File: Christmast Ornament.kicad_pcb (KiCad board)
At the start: 2 copper layers, 98.8 x 92.8 mm, 3 parts

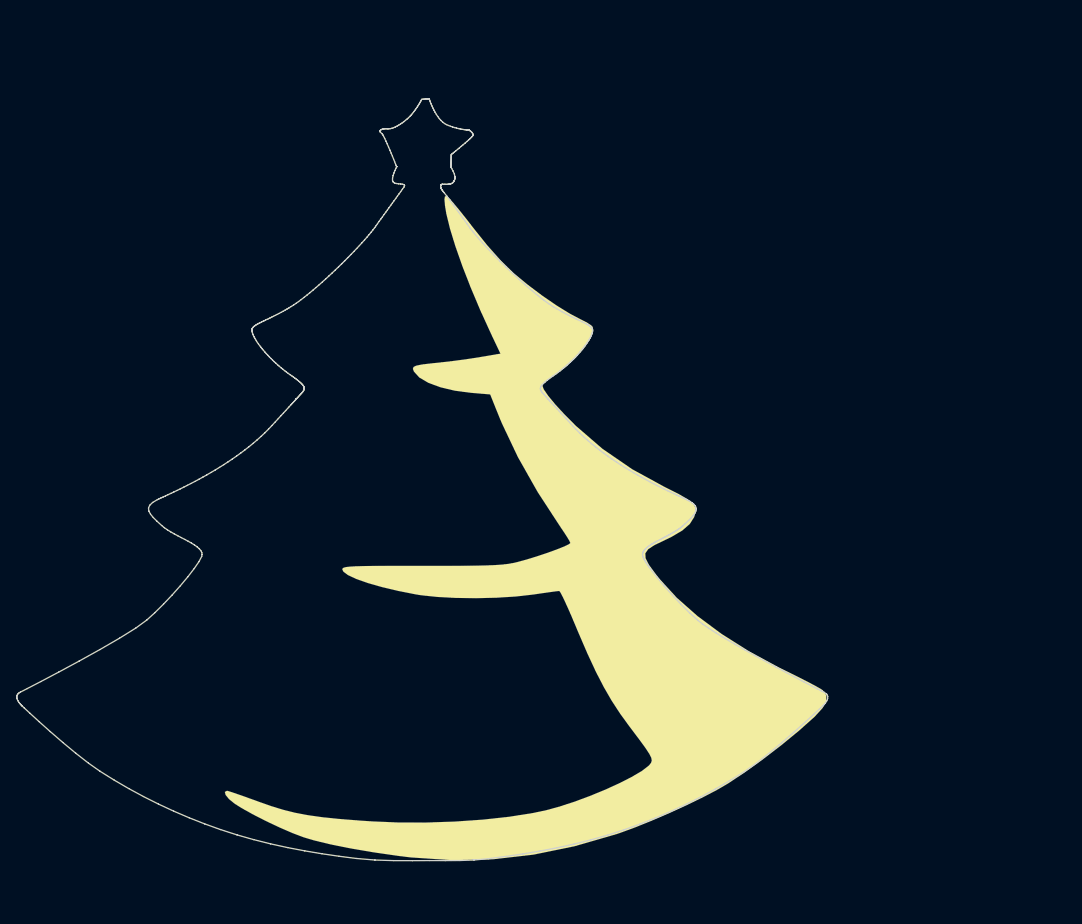
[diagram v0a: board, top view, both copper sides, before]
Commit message: First attempt to distribute components
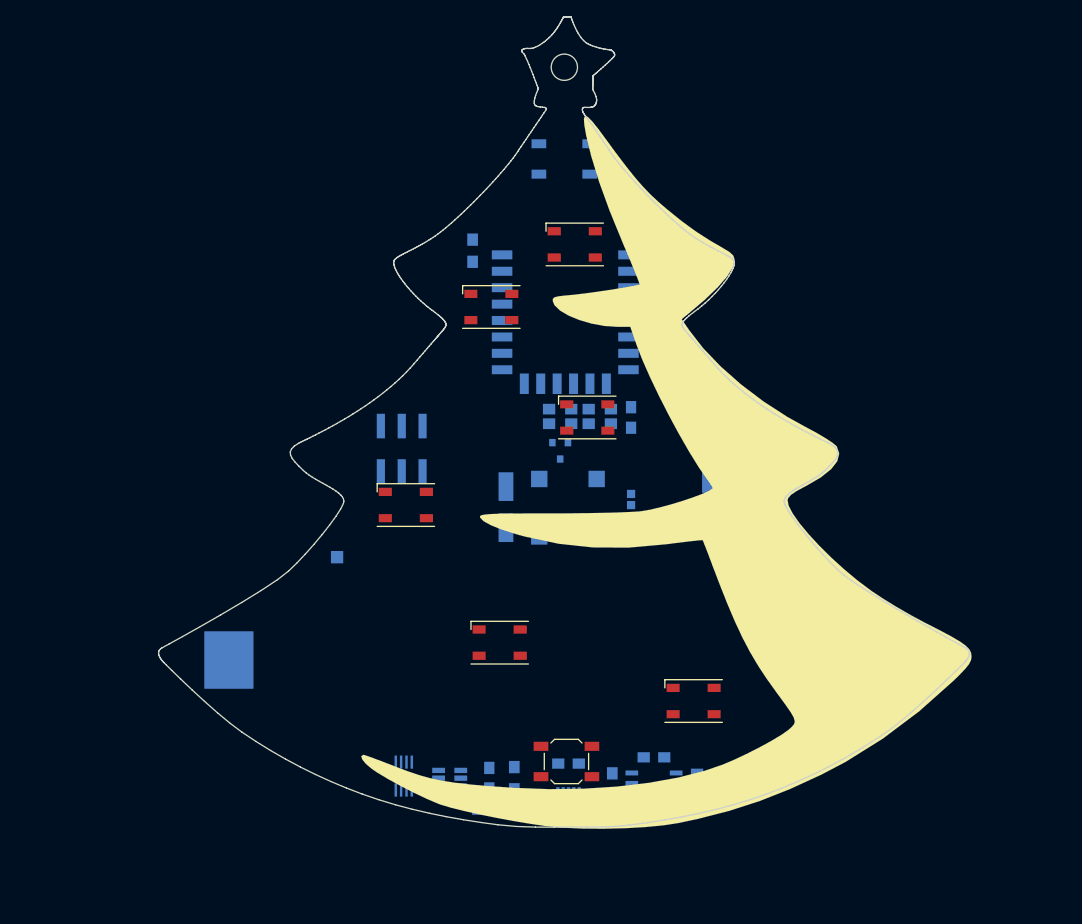
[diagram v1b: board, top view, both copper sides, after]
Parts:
- added BT1: Battery_Cell, MisModulos:18650_SMD_Case, B.Cu at (208.3, 105.7)
- added BZ1: Buzzer, MisModulos:Buzzer_8.5x8.5mm, B.Cu at (164.3, 101.9)
- added C1: 10uF, Capacitors_SMD:C_0805_HandSoldering, B.Cu at (168.7, 128.8)
- added C2: 10uF, Capacitors_SMD:C_0805_HandSoldering, B.Cu at (179.1, 128.0)
- added C3: 0.1uF, Capacitors_SMD:C_0805_HandSoldering, B.Cu at (159.0, 130.6)
- added C4: 1uF, Capacitors_SMD:C_0805_HandSoldering, B.Cu at (190.5, 95.8)
- added C5: 22uF, Capacitors_Tantalum_SMD:CP_Tantalum_Case-A_EIA-3216-18_Hand, B.Cu at (185.7, 92.2)
- added C6: 10uF, Capacitors_SMD:C_0805_HandSoldering, B.Cu at (176.3, 86.6)
- added D1: LED, LEDs:LED_0805, B.Cu at (190.5, 131.3)
- added D2: LED, LEDs:LED_0805, B.Cu at (190.5, 129.3)
- added D3: M7, Diodes_SMD:D_SMA_Handsoldering, B.Cu at (161.0, 97.5)
- added J1: USB_OTG, MisModulos:MicroUSB, B.Cu at (168.7, 135.0)
- added J2: CONN_01X06, Pin_Headers:Pin_Header_Straight_2x03_Pitch2.54mm_SMD, B.Cu at (148.3, 90.4)
- added JP1: Jumper_NC_Dual, MisModulos:Jumper_2-NC, B.Cu at (176.3, 97.3)
- added Q1: 8205A, Housings_SSOP:SSOP-8_2.95x2.8mm_Pitch0.65mm, B.Cu at (148.6, 130.3)
- added Q2: SI2302, TO_SOT_Packages_SMD:SOT-23, B.Cu at (179.8, 74.2)
- added Q3: BC817, TO_SOT_Packages_SMD:SOT-23, B.Cu at (167.6, 90.7)
- added R1: 100, Resistors_SMD:R_0805_HandSoldering, B.Cu at (162.1, 130.6)
- added R10: 10k, Resistors_SMD:R_0805_HandSoldering, B.Cu at (157.0, 66.3)
- added R11: 470, Resistors_SMD:R_0805_HandSoldering, B.Cu at (167.6, 85.6)
- added R12: 10K, Resistors_SMD:R_0805_HandSoldering, B.Cu at (167.6, 87.4)
- added R13: 10K, Resistors_SMD:R_0805_HandSoldering, B.Cu at (180.3, 77.5)
- added R2: 1k, Resistors_SMD:R_0805_HandSoldering, B.Cu at (185.7, 132.1)
- added R3: 1k, Resistors_SMD:R_0805_HandSoldering, B.Cu at (185.7, 130.0)
- added R4: 1k2, Resistors_SMD:R_0805_HandSoldering, B.Cu at (174.0, 131.3)
- added R5: 1k, Resistors_SMD:R_0805_HandSoldering, B.Cu at (159.0, 134.4)
- added R6: 10k, Resistors_SMD:R_0805_HandSoldering, B.Cu at (180.6, 69.3)
- added R7: 10k, Resistors_SMD:R_0805_HandSoldering, B.Cu at (172.5, 87.4)
- added R8: 10k, Resistors_SMD:R_0805_HandSoldering, B.Cu at (172.5, 85.6)
- added R9: 10k, Resistors_SMD:R_0805_HandSoldering, B.Cu at (180.3, 65.5)
- added REF**: MountingHole_3.2mm_M3, Mounting_Holes:MountingHole_3.2mm_M3, F.Cu at (168.1, 43.9)
- added SW1: SW_Push, Buttons_Switches_SMD:SW_SPST_SKQG, B.Cu at (168.1, 55.1)
- added SW2: SW_Push, Buttons_Switches_SMD:SW_SPST_SKQG, F.Cu at (168.4, 128.5)
- added TP1: TEST, Measurement_Points:Measurement_Point_Square-SMD-Pad_Small, B.Cu at (194.8, 129.3)
- added TP2: TEST, Measurement_Points:Measurement_Point_Square-SMD-Pad_Small, B.Cu at (195.6, 103.1)
- added TP3: TEST, Measurement_Points:Measurement_Point_Square-SMD-Pad_Small, B.Cu at (191.0, 103.1)
- added TP4: TEST, Measurement_Points:Measurement_Point_Square-SMD-Pad_Small, B.Cu at (140.5, 103.6)
- added U1: TP4056, Housings_SOIC:SOIC-8_3.9x4.9mm_Pitch1.27mm, B.Cu at (179.1, 131.8)
- added U10: WS2812b, LEDs:LED_WS2812B-PLCC4, F.Cu at (183.9, 121.2)
- added U2: HT7833, TO_SOT_Packages_SMD:SOT89-3_Housing_Handsoldering, B.Cu at (191.0, 91.9)
- added U3: DW01, TO_SOT_Packages_SMD:SOT-23-6_Handsoldering, B.Cu at (154.2, 130.6)
- added U4: ESP-12E, MisModulos:ESP-12E_SMD, B.Cu at (175.3, 66.8)
- added U5: WS2812b, LEDs:LED_WS2812B-PLCC4, F.Cu at (169.4, 65.5)
- added U6: WS2812b, LEDs:LED_WS2812B-PLCC4, F.Cu at (159.3, 73.2)
- added U7: WS2812b, LEDs:LED_WS2812B-PLCC4, F.Cu at (170.9, 86.6)
- added U8: WS2812b, LEDs:LED_WS2812B-PLCC4, F.Cu at (148.8, 97.3)
- added U9: WS2812b, LEDs:LED_WS2812B-PLCC4, F.Cu at (160.3, 114.0)
- moved G*** 33.4 mm to (138.9, 91.7)
- moved G*** 19.6 mm to (168.4, 43.4)
- moved G*** 18.6 mm to (180.6, 93.2)
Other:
- board size 98.8 x 92.8 mm -> 98.8 x 98.7 mm
- board text added: "Revisar pines esp12 ¿Desplazar DW01 y 8205?"

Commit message: PCB routed
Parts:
- removed the REF** at (168.1, 43.9)
- added 3V3: TEST, Measurement_Points:Measurement_Point_Square-SMD-Pad_Small, B.Cu at (183.9, 89.4)
- added GND: TEST, Measurement_Points:Measurement_Point_Square-SMD-Pad_Small, B.Cu at (161.8, 134.9)
- added REF**: MountingHole_2.7mm_M2.5, Mounting_Holes:MountingHole_2.7mm_M2.5, F.Cu at (168.1, 43.7)
- R4: value 1k2 -> 2k7
- moved R5 42.1 mm to (146.3, 94.2)
- moved D1 40.4 mm to (150.1, 131.3), turned to 90 degrees
- moved J2 40.0 mm to (168.1, 55.6)
- moved D2 38.4 mm to (152.1, 131.3), turned to 90 degrees
- moved U3 33.8 mm to (144.9, 98.0), turned to 270 degrees
- moved Q1 31.9 mm to (149.1, 98.4)
- moved C3 31.4 mm to (143.7, 103.1), turned to 180 degrees
- moved R1 30.6 mm to (148.4, 103.1), turned to 180 degrees
- moved R2 28.2 mm to (157.5, 132.6), turned to 180 degrees
- moved R3 28.2 mm to (157.5, 130.6), turned to 180 degrees
- moved BAT+ 26.2 mm to (195.8, 129.3)
- moved BAT- 25.7 mm to (140.7, 129.3)
- moved VCC 20.1 mm to (175.5, 134.9)
- moved R8 20.1 mm to (152.6, 82.5), turned to 90 degrees
- moved SW1 19.4 mm to (154.4, 68.8)
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- renumbered TP2 to BAT+, TP4 to BAT-, TP3 to GND, TP1 to VCC
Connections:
- J2 pad 1: +3V3 -> GND
- J2 pad 2: /TxD -> +3V3
- J2 pad 3: /RxD -> /TxD
- J2 pad 5: Net-(J2-Pad5) -> /RxD
- J2 pad 6: GND -> Net-(J2-Pad6)
- U7 pad 2: Net-(U10-Pad4) -> Net-(U7-Pad2)
- U8 pad 4: Net-(U8-Pad4) -> Net-(U7-Pad2)
- U9 pad 2: Net-(U8-Pad4) -> Net-(U10-Pad4)
- U9 pad 4: Net-(U10-Pad2) -> Net-(U8-Pad2)
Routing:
- net GND: track 0.00 -> 331.4 mm, vias 0 -> 4
- net +3V3: track 0.00 -> 223.0 mm, vias 0 -> 2
- net /PIX_GND: track 0.00 -> 149.7 mm, vias 0 -> 1
- net /RST: track 0.00 -> 116.0 mm, vias 0 -> 1
- net /BAT+: track 0.00 -> 110.9 mm, vias 0 -> 2
- net /BAT-: track 0.00 -> 64.2 mm
- net /VCC: track 0.00 -> 64.1 mm
- net /PIX_DATA: track 0.00 -> 38.8 mm, vias 0 -> 1
- net Net-(R3-Pad1): track 0.00 -> 31.1 mm, vias 0 -> 2
- net Net-(R2-Pad1): track 0.00 -> 29.3 mm, vias 0 -> 2
- net Net-(U7-Pad2): track 0.00 -> 26.8 mm
- net Net-(Q3-Pad1): track 0.00 -> 23.1 mm
- net /TxD: track 0.00 -> 22.0 mm
- net /RxD: track 0.00 -> 21.5 mm
- net Net-(U5-Pad2): track 0.00 -> 21.1 mm
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- added copper zone on B.Cu, net GND
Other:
- net class Alimentación added: clearance 0.25, trace_width 0.3, via_dia 0.6, via_drill 0.3
- net class Default: clearance 0.2 -> 0.15; trace_width 0.25 -> 0.15; via_dia 0.6 -> 0.3; via_drill 0.4 -> 0.15
- rule trace_clearance: 0.2 -> 0.15
- rule trace_min: 0.2 -> 0.15
- rule via_min_drill: 0.3 -> 0.15
- rule via_min_size: 0.4 -> 0.3
- board text added: "+"
- board text added: "-"
- board text removed: "Revisar pines esp12 ¿Desplazar DW01 y 8205?"

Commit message: PCB designed and gerbers
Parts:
- added C10: 0.1uF, Capacitors_SMD:C_0805_HandSoldering, F.Cu at (149.5, 92.5)
- added C11: 0.1uF, Capacitors_SMD:C_0805_HandSoldering, F.Cu at (160.4, 109.9)
- added C12: 0.1uF, Capacitors_SMD:C_0805_HandSoldering, F.Cu at (182.1, 116.1)
- added C7: 0.1uF, Capacitors_SMD:C_0805_HandSoldering, F.Cu at (168.0, 50.3)
- added C8: 0.1uF, Capacitors_SMD:C_0805_HandSoldering, F.Cu at (159.9, 67.4)
- added C9: 0.1uF, Capacitors_SMD:C_0805_HandSoldering, F.Cu at (169.6, 82.7)
- added G***: LOGO, MisModulos:MerryChristmas, F.Cu at (141.9, 113.3)
- C5: value 22uF -> 2.2uF
- TP1: renamed from VCC; value TEST -> VCC
- TP2, TP6: renamed from GND; value TEST -> GND
- TP3: renamed from BAT+; value TEST -> BAT+
- TP4: renamed from BAT-; value TEST -> BAT-
- TP5: renamed from 3V3; value TEST -> 3V3
- moved G*** 54.7 mm to (195.0, 91.3)
- moved G*** 0.08 mm to (168.4, 43.5)
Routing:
- net +3V3: track 223.0 -> 277.1 mm, vias 2 -> 3
- net /PIX_GND: track 149.7 -> 159.6 mm
- net (no net): track 0.00 -> 5.46 mm, vias 0 -> 2
- net Net-(R3-Pad1): track 31.1 -> 33.2 mm
- net Net-(U7-Pad2): track 26.8 -> 28.8 mm
- net Net-(U5-Pad2): track 21.1 -> 22.5 mm
- added copper zone on F.Cu, net (none)
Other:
- net class Default: via_dia 0.3 -> 0.4; via_drill 0.15 -> 0.2

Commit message: TP4056 ground connection fixed
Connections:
- U1 pad 3: (no net) -> GND
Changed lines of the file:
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@@
 (kicad_pcb (version 4) (host pcbnew 4.0.6+dfsg1-1)
   (general
-    (links 116)
+    (links 117)
     (no_connects 2)
     (area 107.9065 37.751949 229.191501 146.367501)
@@
     (pad 2 smd rect (at -2.7 0.635) (size 1.55 0.6) (layers B.Cu B.Paste B.Mask)
       (net 27 "Net-(R4-Pad1)"))
-    (pad 3 smd rect (at -2.7 -0.635) (size 1.55 0.6) (layers B.Cu B.Paste B.Mask))
+    (pad 3 smd rect (at -2.7 -0.635) (size 1.55 0.6) (layers B.Cu B.Paste B.Mask)
+      (net 6 GND))
     (pad 4 smd rect (at -2.7 -1.905) (size 1.55 0.6) (layers B.Cu B.Paste B.Mask)
       (net 5 /VCC))

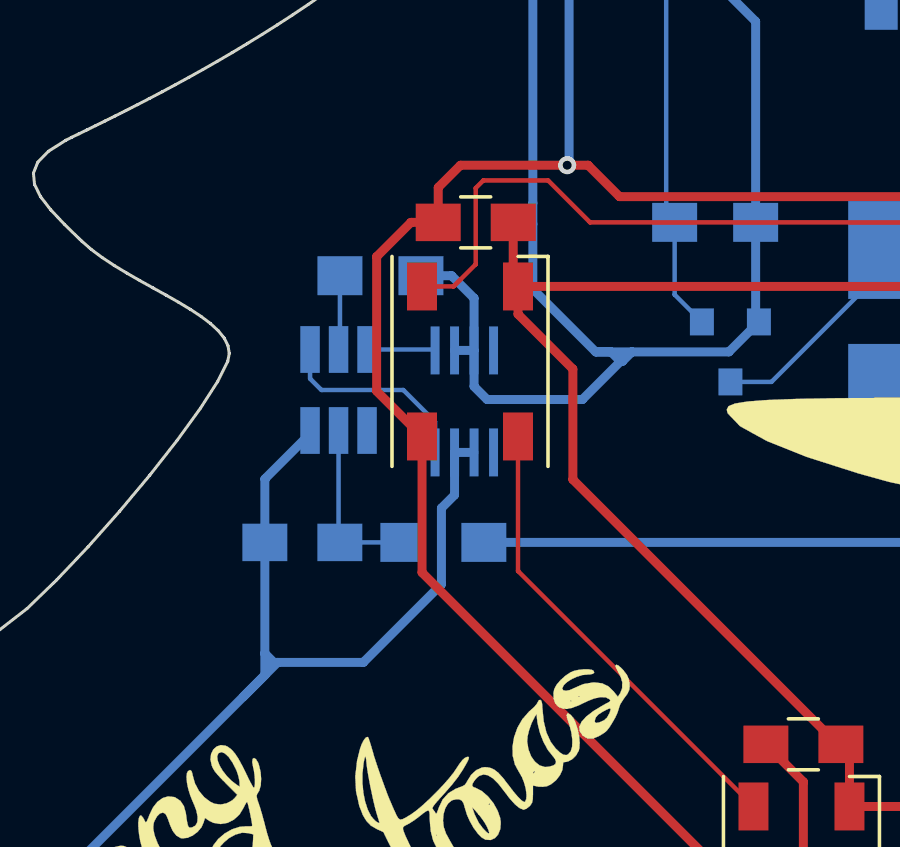
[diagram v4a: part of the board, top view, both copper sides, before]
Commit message: 8205A footprint changed
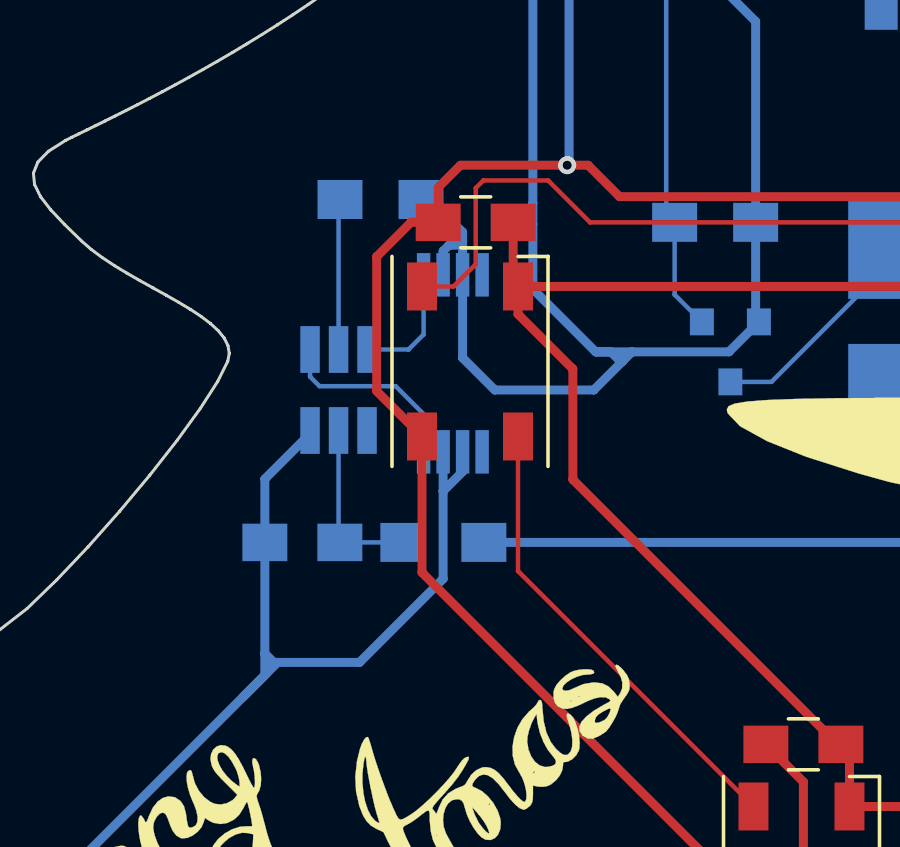
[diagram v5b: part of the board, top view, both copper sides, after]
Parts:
- Q1: footprint Housings_SSOP:SSOP-8_2.95x2.8mm_Pitch0.65mm -> Housings_SSOP:TSSOP-8_4.4x3mm_Pitch0.65mm
- moved R5 2.54 mm to (146.3, 91.7)
- moved Q1 1.33 mm to (148.7, 97.2)
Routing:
- net Net-(R5-Pad1): track 2.48 -> 5.09 mm
- net GND: track 331.4 -> 333.8 mm
- net /OC: track 2.28 -> 4.08 mm
- net /BAT-: track 64.2 -> 64.9 mm

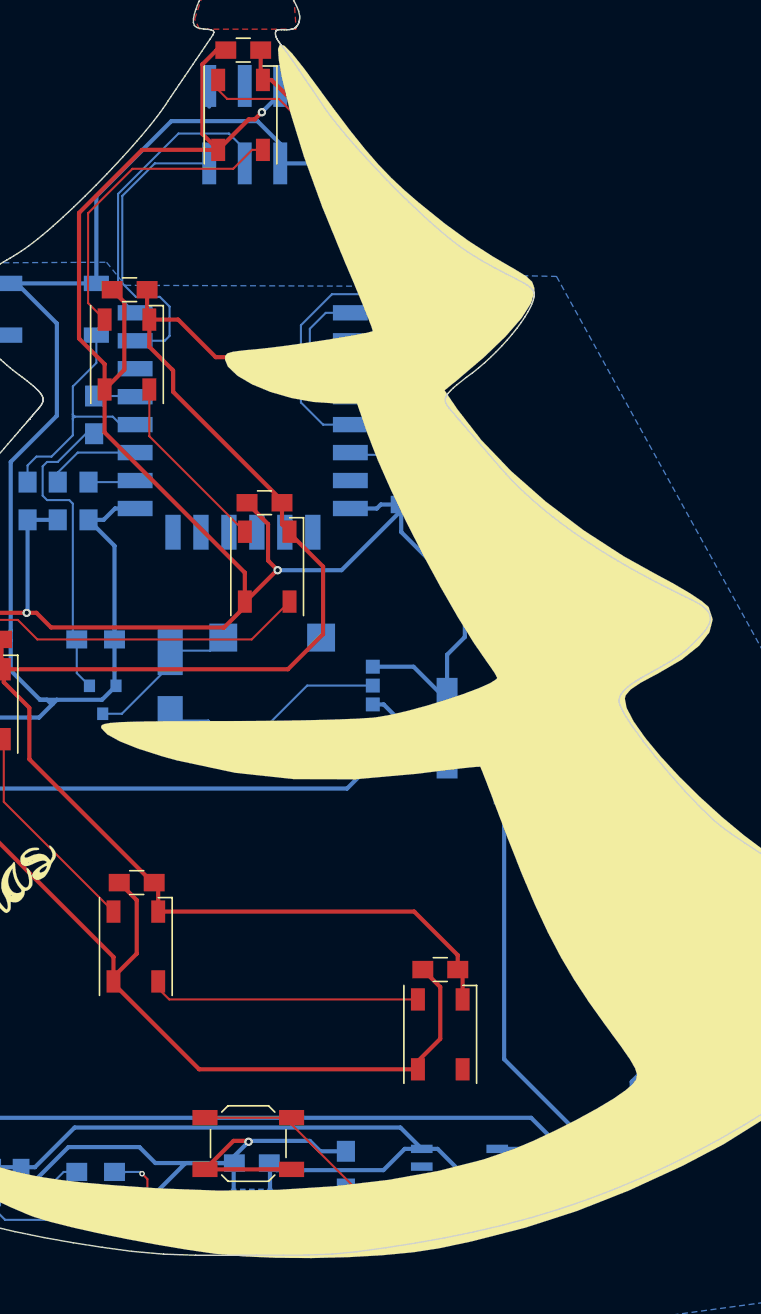
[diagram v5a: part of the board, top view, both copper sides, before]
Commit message: Components added to reset button
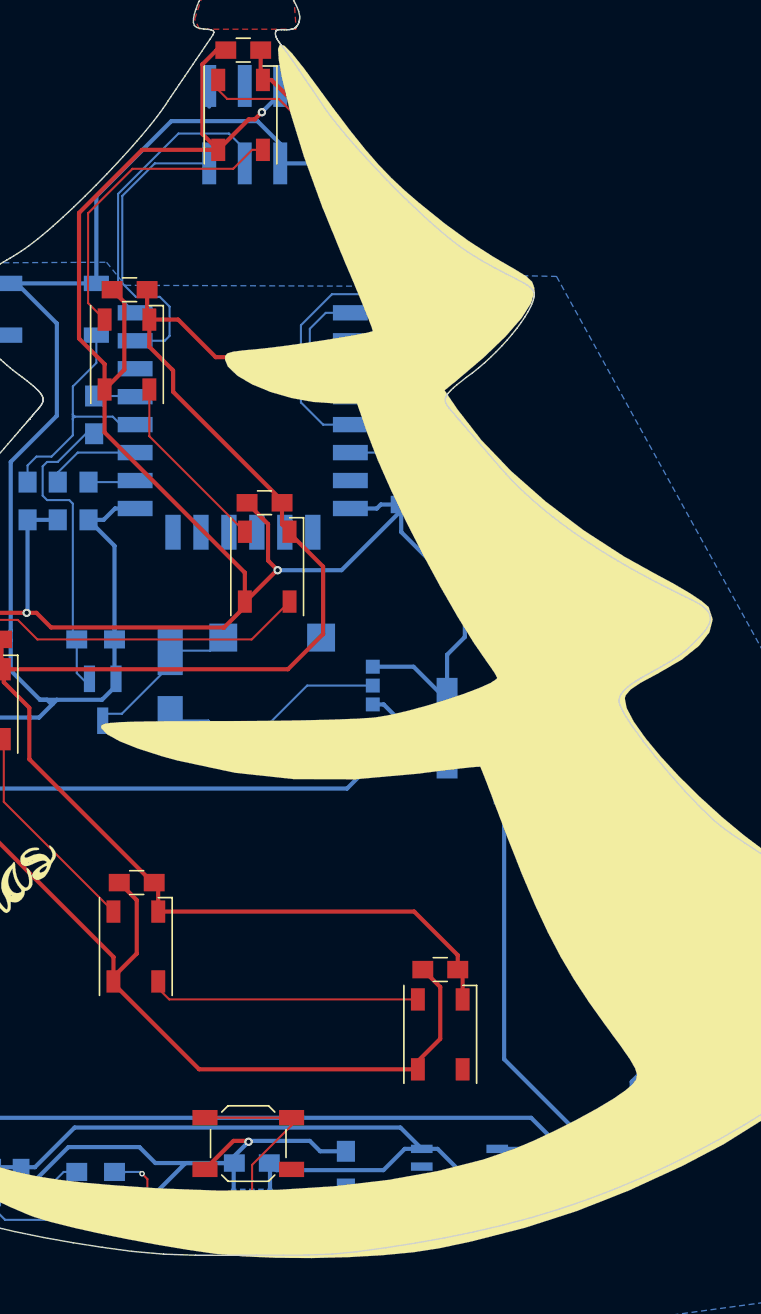
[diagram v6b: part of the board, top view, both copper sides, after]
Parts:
- added C13: 10uF, Capacitors_SMD:C_0805_HandSoldering, B.Cu at (180.1, 64.6)
- added D4: D_Schottky, Diodes_SMD:D_0805, B.Cu at (179.7, 69.3)
- added D5: D_Schottky, Diodes_SMD:D_0805, B.Cu at (186.1, 68.3)
- added R14: 470k, Resistors_SMD:R_0805_HandSoldering, B.Cu at (182.8, 66.9)
- Q2, Q3: footprint TO_SOT_Packages_SMD:SOT-23 -> TO_SOT_Packages_SMD:SOT-23_Handsoldering
- moved R9 3.71 mm to (183.9, 70.7), turned to 90 degrees
- moved R13 1.02 mm to (180.5, 80.3)
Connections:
- R9 pad 2: /RST -> Net-(D4-Pad1)
- SW2 pad 1: /RST -> Net-(D4-Pad1)
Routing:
- net Net-(D4-Pad1): track 0.00 -> 117.8 mm, vias 0 -> 1
- net /RST: track 116.0 -> 12.8 mm, vias 1 -> 0
- net GND: track 333.8 -> 324.9 mm
- net +3V3: track 277.1 -> 285.6 mm
- net Net-(C13-Pad1): track 0.00 -> 6.30 mm
- net /PIX_GND: track 159.6 -> 161.6 mm
- net /PIX_ON: track 9.44 -> 11.1 mm
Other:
- board text added: "Rx"
- board text added: "Tx"
